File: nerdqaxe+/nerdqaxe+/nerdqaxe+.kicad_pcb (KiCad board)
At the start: 4 copper layers, 89 x 152 mm, 211 parts, among them J1 Barrel_Jack_Switch, J2 Conn_01x06, J3 Conn_01x01, J4 Conn_01x01, M1 Fan_4pin, M2 Fan_4pin, U19 BM1368_mode1, U20 BM1368_mode1, U25 BM1368_mode1, U26 BM1368_mode1, U3 TPS53647, U30 T-Display-S3, U32 EMC2302-1, U33 TXU0102-DCU, U35 TXU0304PW, U36 MCP1824T-1802E, U37 TMP1075, U38 TMP1075, U4 CSD95472Q5MC, U5 CSD95472Q5MC, U6 AP3211, U7 MCP1824T-0802E, U8 25MHz

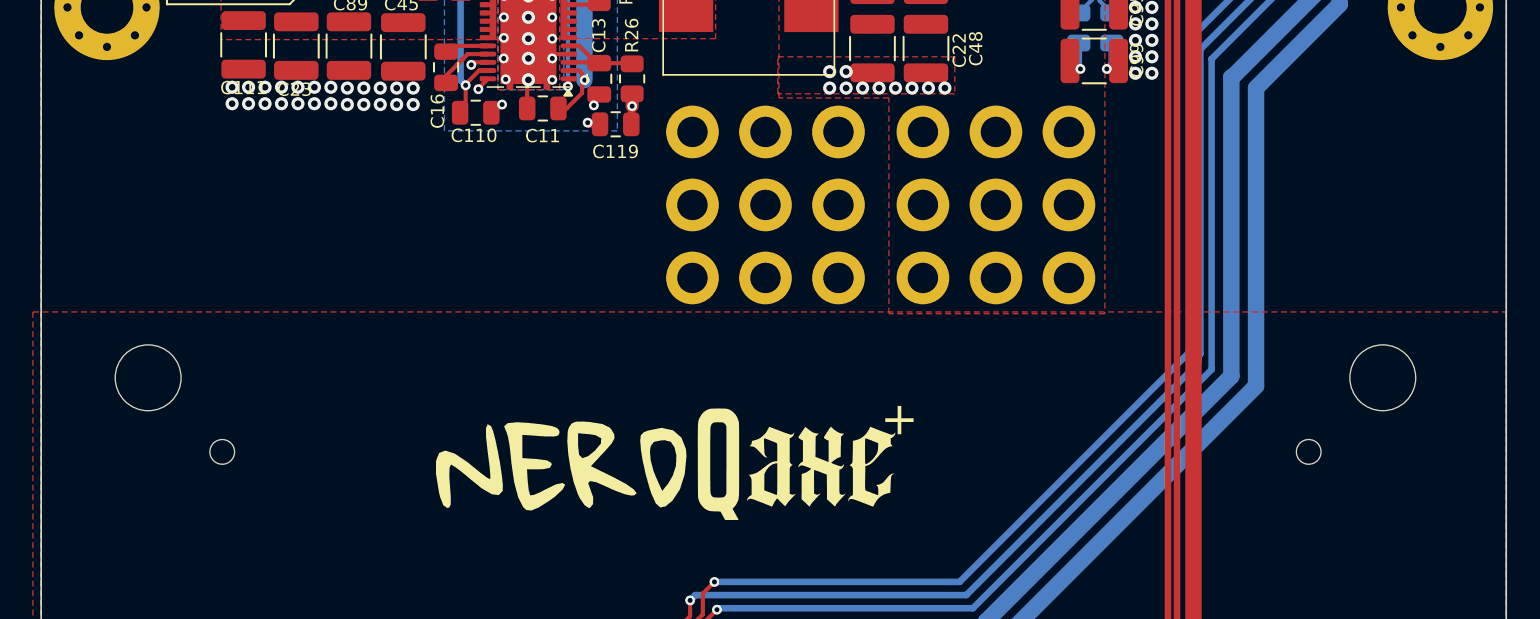
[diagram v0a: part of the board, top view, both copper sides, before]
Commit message: removed big M4 connectors because they were only for the prototypes
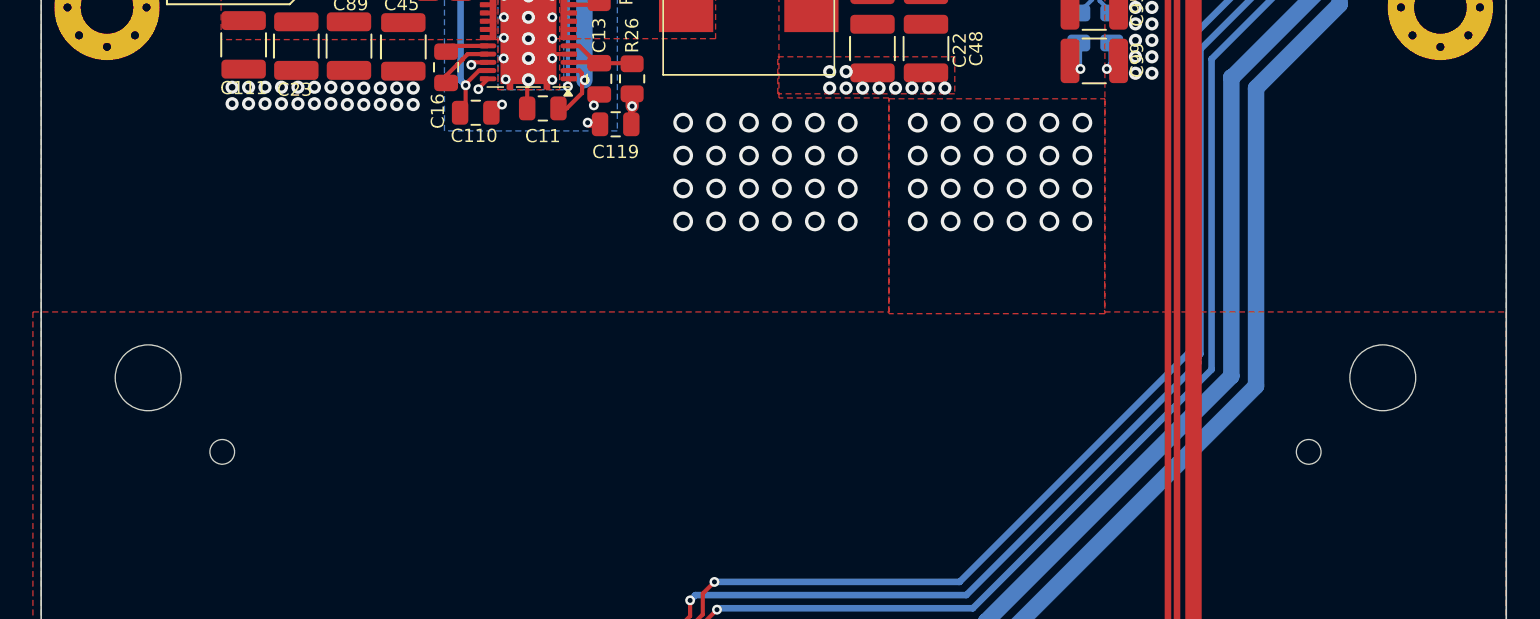
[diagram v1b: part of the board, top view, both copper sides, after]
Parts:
- removed the G*** at (82.5, 92.8)
- removed the G*** at (96.9, 92.8)
- removed J3, J4: Conn_01x01, TerminalBlock_Wuerth:Wuerth_REDCUBE-THR_WP-THRBU_74650194_THR
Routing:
- net GND: vias 314 -> 338
- net +1V2: vias 36 -> 60

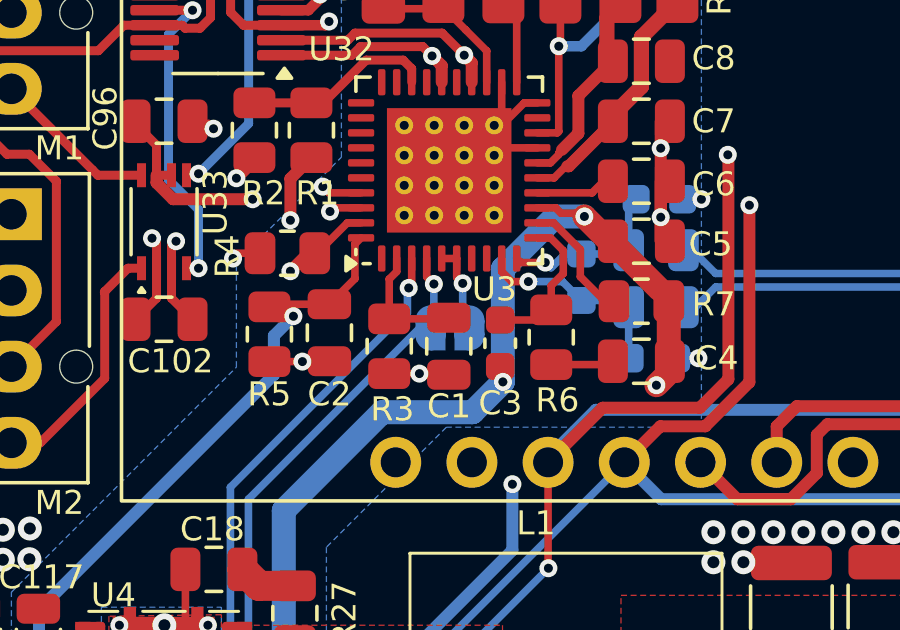
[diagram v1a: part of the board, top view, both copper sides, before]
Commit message: removed ph2-dis solderjumper because it's not needed
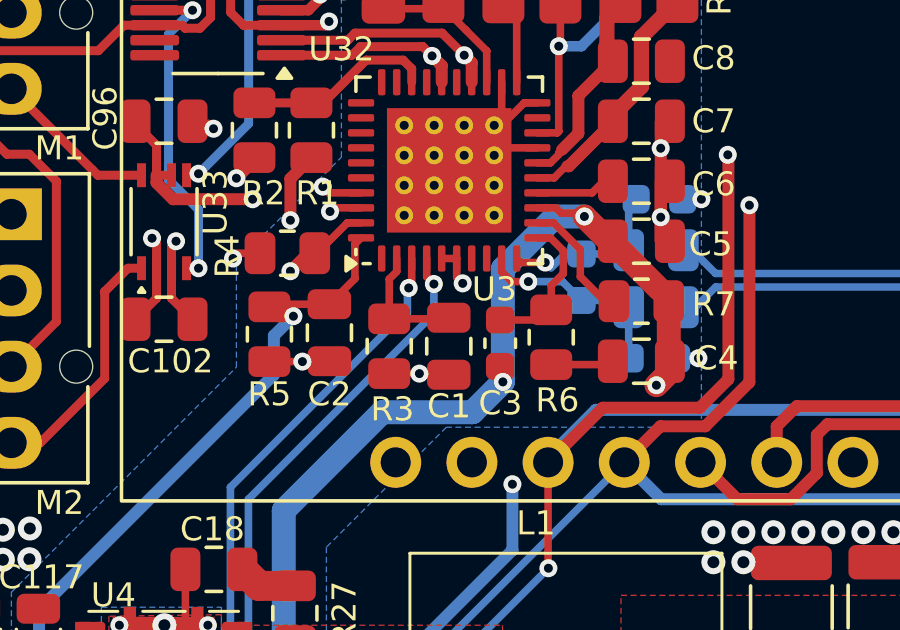
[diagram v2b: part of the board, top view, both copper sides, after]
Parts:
- removed JP3: SolderJumper_2_Open, Jumper:SolderJumper-2_P1.3mm_Open_RoundedPad1.0x1.5mm
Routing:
- net +3V3: track 130.8 -> 129.2 mm
